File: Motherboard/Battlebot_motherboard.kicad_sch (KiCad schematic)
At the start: 5 parts, among them J1 BEC, U1 rp2040-zero, U2 L9958SBTR, U3 L9958SBTR

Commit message: all the pcb stuff
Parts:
- removed U1: rp2040-zero, footprints:rp2040-zero-tht, symbol mcu:rp2040-zero
- removed U2, U3: L9958SBTR, L9958SBTR:SOP80P1410X360-17N, symbol L9958SBTR:L9958SBTR
- added C10, C9: 1uF, Capacitor_SMD:C_0805_2012Metric_Pad1.18x1.45mm_HandSolder, symbol Device:C
- added C11, C12: 100uF, Capacitor_SMD:CP_Elec_3x5.3, symbol Device:C_Polarized
- added C2, C7, C8: 100nF, Capacitor_SMD:C_0805_2012Metric_Pad1.18x1.45mm_HandSolder, symbol Device:C
- added C3, C4, C5, C6: 10nF, Capacitor_SMD:C_0805_2012Metric_Pad1.18x1.45mm_HandSolder, symbol Device:C
- added J2: Reciever, Connector_PinHeader_2.54mm:PinHeader_1x03_P2.54mm_Vertical, symbol Connector:Conn_01x03_Socket
- added J3: 12Vin, library:2_Wire, symbol Connector:Conn_01x02_Socket
- added J4, J5: Conn_01x02_Socket, library:2_Wire, symbol Connector:Conn_01x02_Socket
- added J6: Fan connector, Connector_JST:JST_PH_S2B-PH-K_1x02_P2.00mm_Horizontal, symbol Connector:Conn_01x02_Socket
- added JP1, JP2: 0ohm, Resistor_SMD:R_1206_3216Metric_Pad1.30x1.75mm_HandSolder, symbol Device:R
- added R1, R2, R5, R6: 10kohm, Resistor_SMD:R_0805_2012Metric_Pad1.20x1.40mm_HandSolder, symbol Device:R
- added R3, R4: 22kohm, Resistor_SMD:R_0805_2012Metric_Pad1.20x1.40mm_HandSolder, symbol Device:R
- added U2, U3: L9958SBTR, POWERSO16_STM, symbol 2024-12-25_01-36-40:L9958SBTR
- added U4: XIAO-RP2040-SMD, footprints:XIAO-RP2040-SMD, symbol Seeed_Studio_XIAO_Series:XIAO-RP2040-SMD
- C1: value C -> 100nF; footprint (none) -> Capacitor_SMD:C_0805_2012Metric_Pad1.18x1.45mm_HandSolder
- J1: footprint (none) -> Connector_PinHeader_2.54mm:PinHeader_1x03_P2.54mm_Vertical
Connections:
- net GND: now also C1.2, C10.2, C11.2, C12.2, C2.2, C7.2, C8.2, C9.2, J2.3 (Pin_3), J3.2 (Pin_2), J6.2 (Pin_2), R3.2, R4.2, R5.2, R6.2, U2.1 (GND), U2.8 (PGND), U3.1 (GND), U3.8 (PGND), U4.16 (GND), U4.20 (GND); no longer J1.2 (Pin_2)
- net +5V: now reaches J1.1 (Pin_1)
- net +5V: now also C7.1, C8.1, J2.1 (Pin_1), J6.1 (Pin_1), R1.2, R2.2, U2.16 (VDD), U3.16 (VDD), U4.14 (5V)
- net PWM3: now reaches J1.3 (Pin_3)
- net PWM3: now also U4.1 (GPIO26_A0_D0)
- net at C1.1: now also U2.4 (CP)
- new net: C5.1, J4.1 (Pin_1)
- new net: C3.2, J4.2 (Pin_2)
- new net: C5.2, U2.10 (OUT2)
- new net: J1.2 (Pin_2), U4.13 (GND)
- new net: C6.2, U3.10 (OUT2)
- new net: R6.1, U3.12 (REXT)
- new net: C2.1, U3.4 (CP)
- new net: C4.1, U3.6 (OUT1)
- new net: R4.1, U3.9 (EN)
- new net: R3.1, U2.9 (EN)
- new net: R5.1, U2.12 (REXT)
- new net: C3.1, U2.6 (OUT1)
- new net: C4.2, J5.2 (Pin_2)
- new net: C6.1, J5.1 (Pin_1)
- new net +12V: C10.1, C11.1, C12.1, C9.1, J3.1 (Pin_1), U2.13 (VS), U3.13 (VS)
- new net 1SO: U2.14 (SI), U3.2 (SO)
- new net CS: U2.3 (CS), U3.3 (CS), U4.8 (GPIO1_D7_CSn_RX)
- new net DI1: R2.1, U3.7 (DI)
- new net DI2: R1.1, U2.7 (DI)
- new net DIR1: U3.5 (DIR), U4.5 (GPIO6_D4_SDA)
- new net DIR2: U2.5 (DIR), U4.6 (GPIO7_D5_SCL)
- new net PPM: J2.2 (Pin_2), U4.4 (GPIO29_A3_D3)
- new net PWM1: U3.11 (PWM), U4.2 (GPIO27_A1_D1)
- new net PWM2: U2.11 (PWM), U4.3 (GPIO28_A2_D2)
- new net SCK: U2.15 (SCK), U3.15 (SCK), U4.9 (GPIO2_D8_SCK)
- new net µSI: U2.2 (SO), U4.11 (GPIO3_D10_MOSI)
- new net µSO: U3.14 (SI), U4.10 (GPIO4_D9_MISO)
- no-connect marks 0 -> 7
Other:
- note added: "Brushed Motor Drivers"
- note added: "Microcontroller"
- note added: "Misc. Connectors"

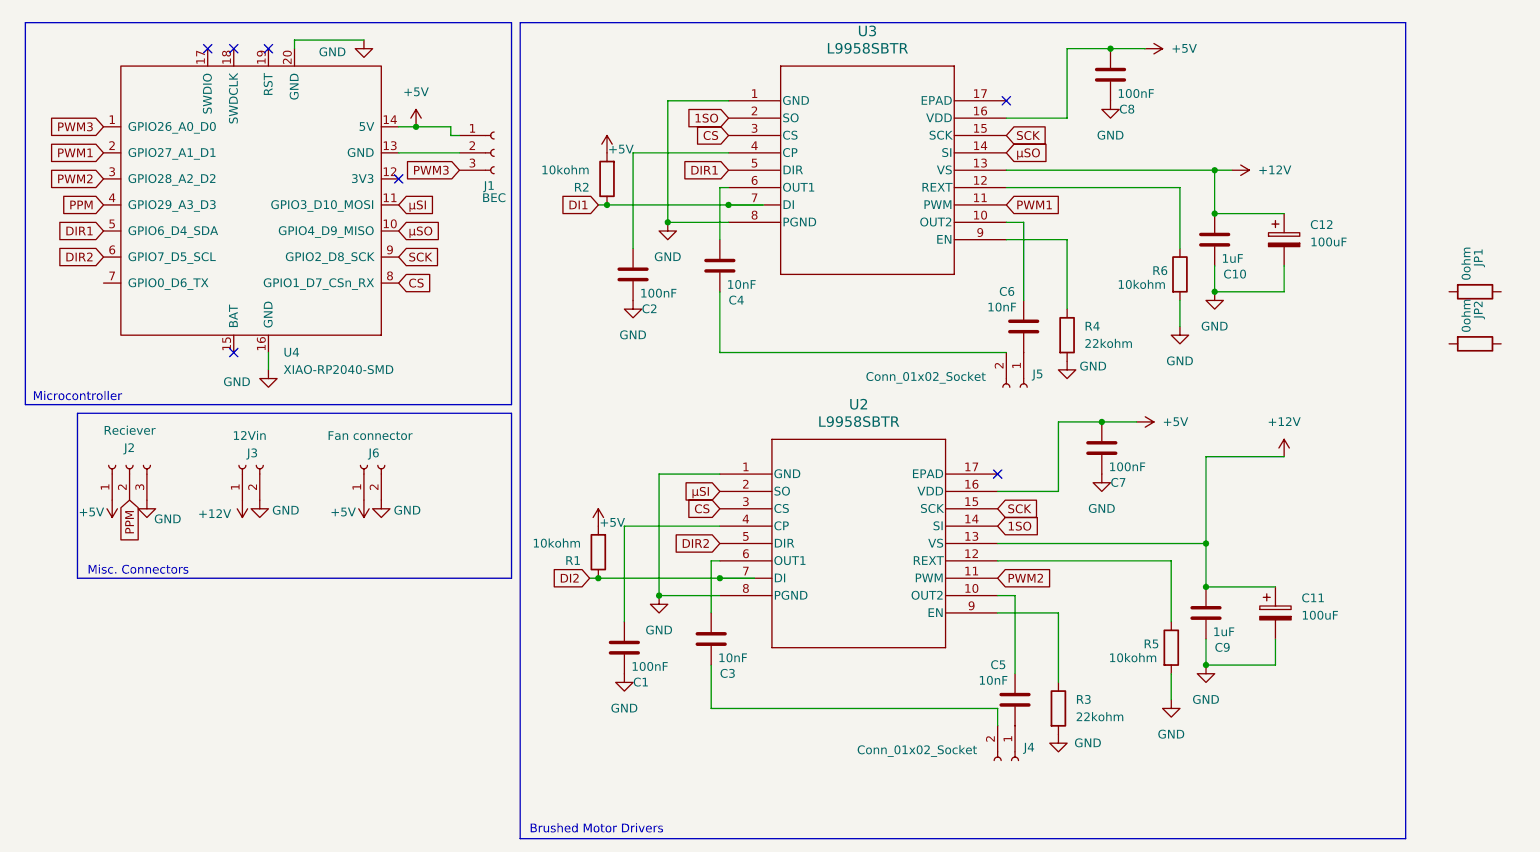
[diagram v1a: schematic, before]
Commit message: Update schematic which was quite wrong in a number of places
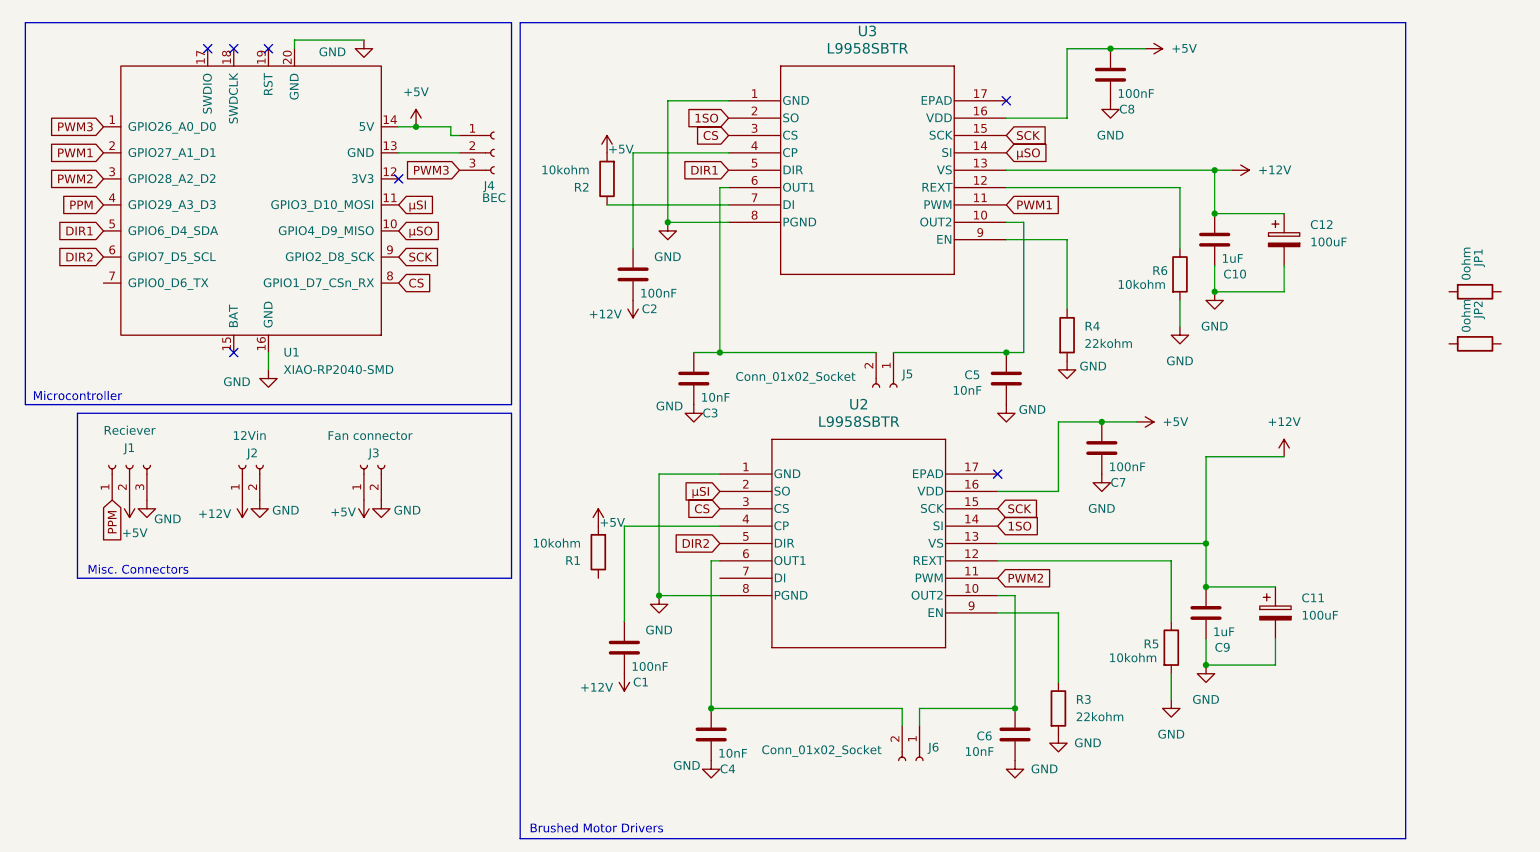
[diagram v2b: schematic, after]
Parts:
- renumbered C4 to C3, C3 to C4, C6 to C5, C5 to C6, J2 to J1, J3 to J2, J6 to J3, J1 to J4, J4 to J6, U4 to U1
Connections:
- net +12V: now also C1.2, C2.2
- net +5V: now also J1.2 (Pin_2); no longer J1.1 (Pin_1)
- net GND: now also C3.2, C4.2, C5.1, C6.1; no longer C1.2, C2.2
- net PPM: now also J1.1 (Pin_1); no longer J1.2 (Pin_2)
- net at J6.1 (Pin_1): now also C6.2, U2.10 (OUT2); no longer C6.1
- net at J6.2 (Pin_2): now also C4.1, U2.6 (OUT1); no longer C4.2
- net at C5.2, U3.10 (OUT2): now also J5.1 (Pin_1)
- net at C3.1, U3.6 (OUT1): now also J5.2 (Pin_2)
- net DI1: no longer names the net of R2.1, U3.7 (DI)
- net DI2: no longer names the net of U2.7 (DI)
- net DI2: no longer R1.1
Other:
- moved on the sheet: C3, C4, C5, C6, J5, J6

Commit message: nightmare routing job
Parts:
- J5, J6: footprint library:2_Wire -> Connector_JST:JST_PH_S2B-PH-K_1x02_P2.00mm_Horizontal
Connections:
- net GND: now also U2.17 (EPAD), U3.17 (EPAD)
- net at U2.7 (DI): now also R1.1
- no-connect marks 7 -> 5
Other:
- moved on the sheet: R1
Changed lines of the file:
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@@
 	)
 	(no_connect
-		(at 154.94 81.28)
-	)
-	(no_connect
-		(at 156.21 26.67)
-	)
-	(no_connect
 		(at 48.26 19.05)
 	)
@@
 	(wire
 		(pts
+			(xy 96.52 96.52) (xy 114.3 96.52)
+		)
+		(stroke
+			(width 0)
+			(type default)
+		)
+	)
+	(wire
+		(pts
 			(xy 110.49 63.5) (xy 114.3 63.5)
 		)
@@
 			)
 		)
-		(property "Footprint" "library:2_Wire"
+		(property "Footprint" "Connector_JST:JST_PH_S2B-PH-K_1x02_P2.00mm_Horizontal"
 			(at 143.51 123.19 0)
 			(effects
@@
 	(symbol
 		(lib_id "Device:R")
-		(at 96.52 92.71 180)
+		(at 96.52 92.71 0)
+		(mirror x)
 		(unit 1)
 		(exclude_from_sim no)
@@
 		(dnp no)
 		(property "Reference" "R1"
-			(at 93.98 93.9801 0)
+			(at 99.06 93.9801 0)
 			(effects
 				(font
@@
 		)
 		(property "Value" "10kohm"
-			(at 93.98 91.4401 0)
+			(at 99.06 91.4401 0)
 			(effects
 				(font
@@
 		)
 		(property "Footprint" "Resistor_SMD:R_0805_2012Metric_Pad1.20x1.40mm_HandSolder"
-			(at 98.298 92.71 90)
+			(at 94.742 92.71 90)
 			(effects
 				(font
@@
 	)
 	(symbol
+		(lib_id "power:GND")
+		(at 156.21 26.67 180)
+		(unit 1)
+		(exclude_from_sim no)
+		(in_bom yes)
+		(on_board yes)
+		(dnp no)
+		(fields_autoplaced yes)
+		(property "Reference" "#PWR032"
+			(at 156.21 20.32 0)
+			(effects
+				(font
+					(size 1.27 1.27)
+				)
+				(hide yes)
+			)
+		)
+		(property "Value" "GND"
+			(at 156.21 21.59 0)
+			(effects
+				(font
+					(size 1.27 1.27)
+				)
+			)
+		)
+		(property "Footprint" ""
+			(at 156.21 26.67 0)
+			(effects
+				(font
+					(size 1.27 1.27)
+				)
+				(hide yes)
+			)
+		)
+		(property "Datasheet" ""
+			(at 156.21 26.67 0)
+			(effects
+				(font
+					(size 1.27 1.27)
+				)
+				(hide yes)
+			)
+		)
+		(property "Description" "Power symbol creates a global label with name \"GND\" , ground"
+			(at 156.21 26.67 0)
+			(effects
+				(font
+					(size 1.27 1.27)
+				)
+				(hide yes)
+			)
+		)
+		(pin "1"
+		)
+		(instances
+			(project ""
+				(path "/1991c32d-5f82-4678-bacc-ea14347159fa"
+					(reference "#PWR032")
+					(unit 1)
+				)
+			)
+		)
+	)
+	(symbol
 		(lib_id "Device:C")
 		(at 185.42 101.6 0)
@@
 			)
 		)
-		(property "Footprint" "library:2_Wire"
+		(property "Footprint" "Connector_JST:JST_PH_S2B-PH-K_1x02_P2.00mm_Horizontal"
 			(at 139.7 68.58 0)
 			(effects
@@
 					(unit 1)
 				)
+			)
+		)
+	)
+	(symbol
+		(lib_id "power:GND")
+		(at 154.94 81.28 180)
+		(unit 1)
+		(exclude_from_sim no)
+		(in_bom yes)
+		(on_board yes)
+		(dnp no)
+		(fields_autoplaced yes)
+		(property "Reference" "#PWR033"
+			(at 154.94 74.93 0)
+			(effects
+				(font
+					(size 1.27 1.27)
+				)
+				(hide yes)
+			)
+		)
+		(property "Value" "GND"
+			(at 154.94 76.2 0)
+			(effects
+				(font
+					(size 1.27 1.27)
+				)
+			)
+		)
+		(property "Footprint" ""
+			(at 154.94 81.28 0)
+			(effects
+				(font
+					(size 1.27 1.27)
+				)
+				(hide yes)
+			)
+		)
+		(property "Datasheet" ""
+			(at 154.94 81.28 0)
+			(effects
+				(font
+					(size 1.27 1.27)
+				)
+				(hide yes)
+			)
+		)
+		(property "Description" "Power symbol creates a global label with name \"GND\" , ground"
+			(at 154.94 81.28 0)
+			(effects
+				(font
+					(size 1.27 1.27)
+				)
+				(hide yes)
+			)
+		)
+		(pin "1"
+		)
+		(instances
+			(project "Battlebot_motherboard"
+				(path "/1991c32d-5f82-4678-bacc-ea14347159fa"
+					(reference "#PWR033")
+					(unit 1)
+				)

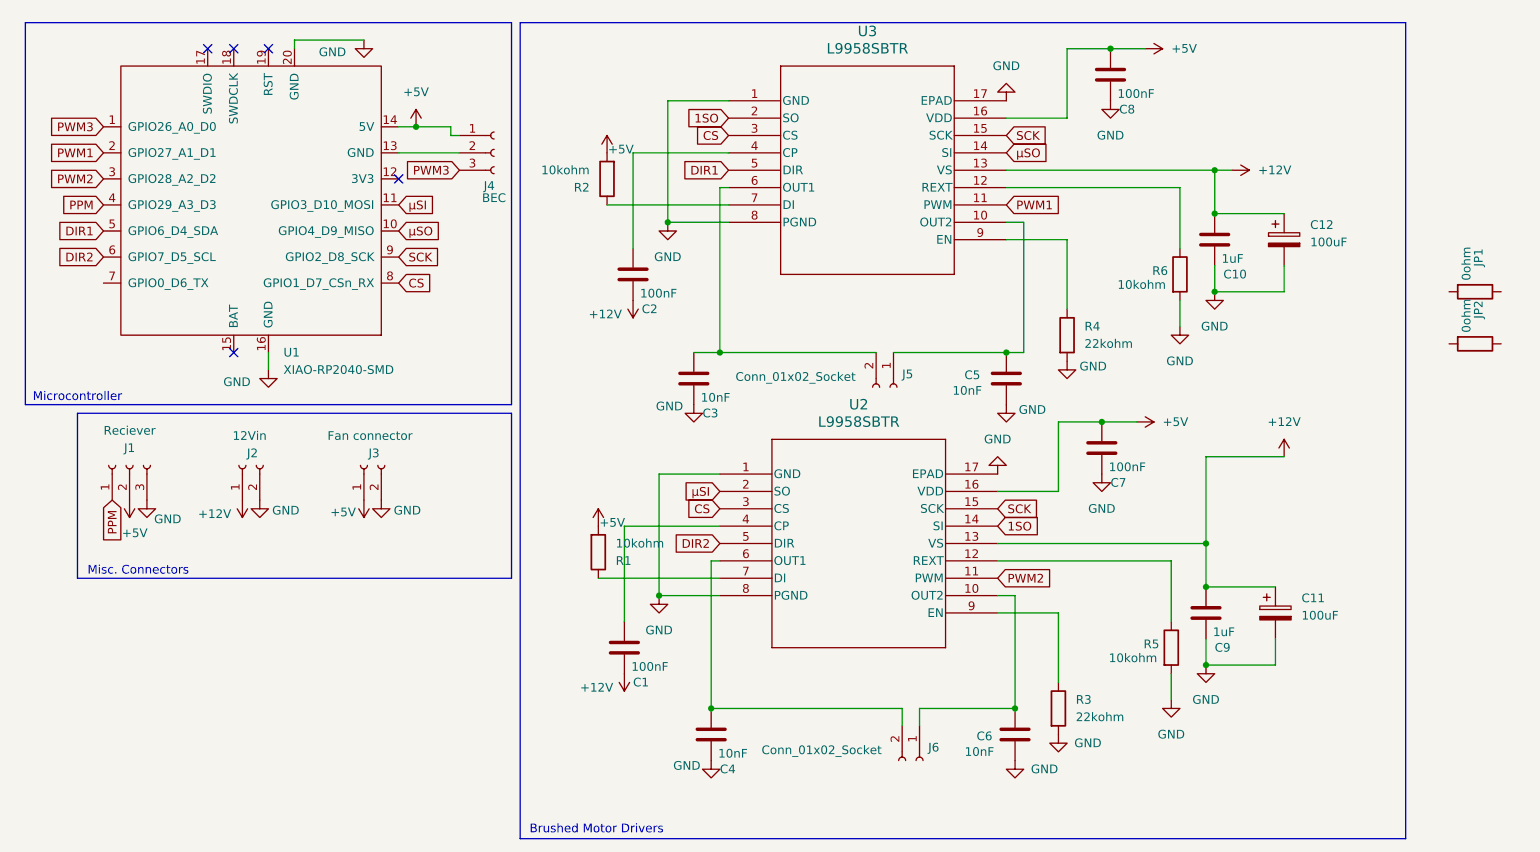
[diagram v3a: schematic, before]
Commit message: reroute using 2 layers and fix 1 connector
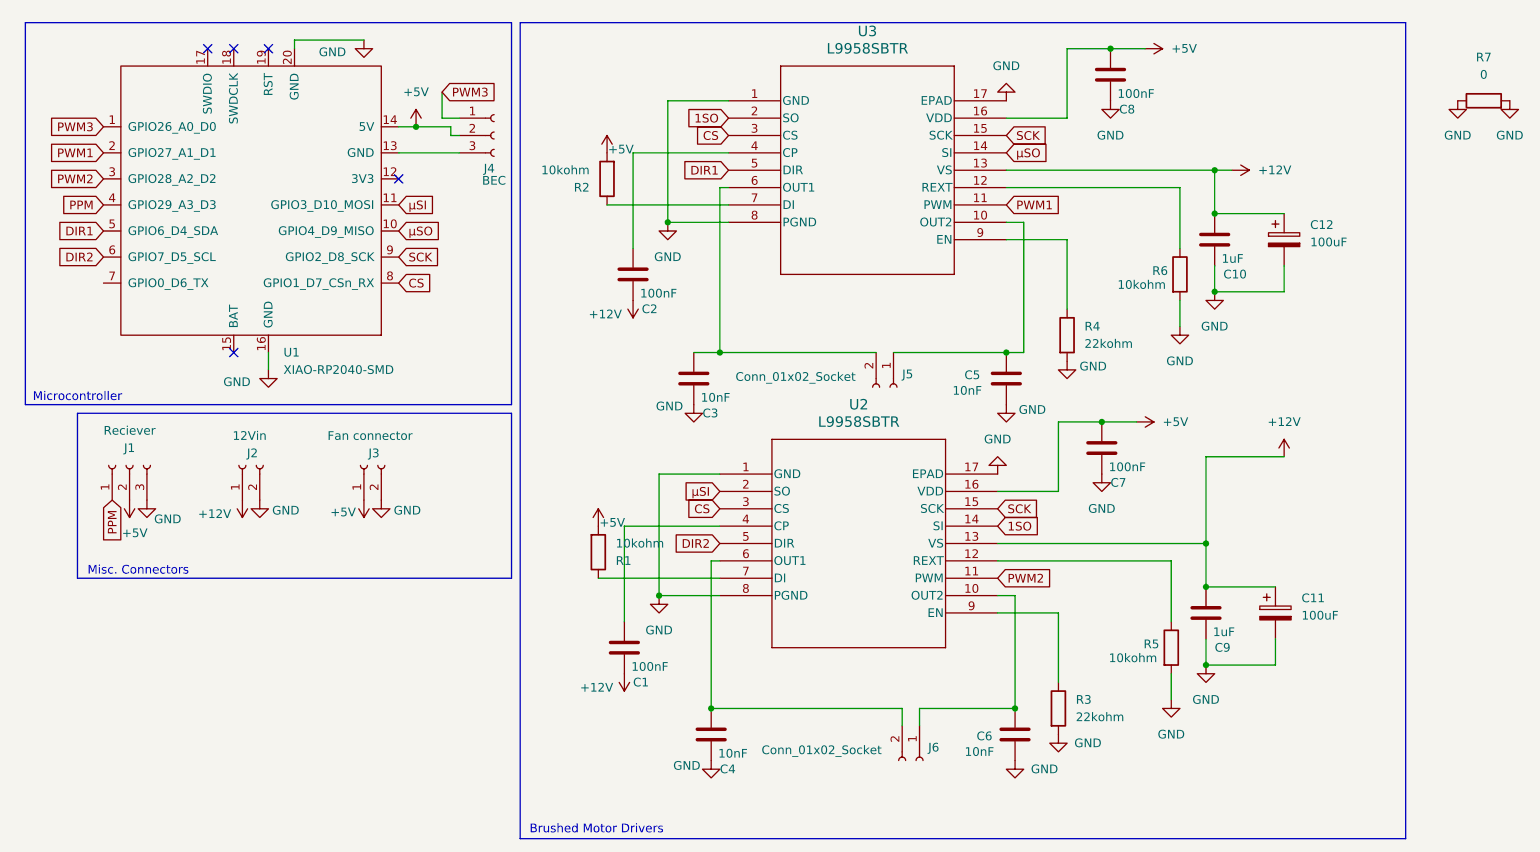
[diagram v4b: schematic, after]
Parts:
- removed JP1, JP2: 0ohm, Resistor_SMD:R_1206_3216Metric_Pad1.30x1.75mm_HandSolder, symbol Device:R
- added R7: 0, Resistor_THT:R_Axial_DIN0204_L3.6mm_D1.6mm_P5.08mm_Vertical, symbol Device:R
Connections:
- net +5V: now also J4.2 (Pin_2); no longer J4.1 (Pin_1)
- net GND: now also R7.1, R7.2
- net PWM3: now also J4.1 (Pin_1); no longer J4.3 (Pin_3)
- net at U1.13 (GND): now also J4.3 (Pin_3); no longer J4.2 (Pin_2)
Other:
- moved on the sheet: J4

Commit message: new cap footprint and rerouting for it
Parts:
- C11, C12: footprint Capacitor_SMD:CP_Elec_3x5.3 -> footprints:CAP_UCD_4X5P8_NCH
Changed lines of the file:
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@@
 			)
 		)
-		(property "Footprint" "Capacitor_SMD:CP_Elec_3x5.3"
+		(property "Footprint" "footprints:CAP_UCD_4X5P8_NCH"
 			(at 196.5452 105.41 0)
 			(effects
@@
 			)
 		)
-		(property "Footprint" "Capacitor_SMD:CP_Elec_3x5.3"
+		(property "Footprint" "footprints:CAP_UCD_4X5P8_NCH"
 			(at 197.8152 50.8 0)
 			(effects

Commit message: fix traces and stuff
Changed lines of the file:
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@@
 (kicad_sch
-	(version 20231120)
+	(version 20250114)
 	(generator "eeschema")
-	(generator_version "8.0")
+	(generator_version "9.0")
 	(paper "A4")
+	(rectangle
+		(start 20.32 72.39)
+		(end 83.82 96.52)
+		(stroke
+			(width 0)
+			(type default)
+		)
+		(fill
+			(type none)
+		)
+	)
+	(rectangle
+		(start 85.09 15.24)
+		(end 214.63 134.62)
+		(stroke
+			(width 0)
+			(type default)
+		)
+		(fill
+			(type none)
+		)
+	)
+	(rectangle
+		(start 12.7 15.24)
+		(end 83.82 71.12)
+		(stroke
+			(width 0)
+			(type default)
+		)
+		(fill
+			(type none)
+		)
+	)
+	(text "Misc. Connectors"
+		(exclude_from_sim no)
+		(at 29.21 95.504 0)
+		(effects
+			(font
+				(size 1.27 1.27)
+			)
+		)
+	)
+	(text "Microcontroller"
+		(exclude_from_sim no)
+		(at 20.32 70.104 0)
+		(effects
+			(font
+				(size 1.27 1.27)
+			)
+		)
+	)
+	(text "Brushed Motor Drivers\n"
+		(exclude_from_sim no)
+		(at 96.266 133.35 0)
+		(effects
+			(font
+				(size 1.27 1.27)
+			)
+		)
+	)
 	(junction
 		(at 171.45 19.05)
@@
 		)
 	)
-	(rectangle
-		(start 20.32 72.39)
-		(end 83.82 96.52)
-		(stroke
-			(width 0)
-			(type default)
-		)
-		(fill
-			(type none)
-		)
-	)
-	(rectangle
-		(start 85.09 15.24)
-		(end 214.63 134.62)
-		(stroke
-			(width 0)
-			(type default)
-		)
-		(fill
-			(type none)
-		)
-	)
-	(rectangle
-		(start 12.7 15.24)
-		(end 83.82 71.12)
-		(stroke
-			(width 0)
-			(type default)
-		)
-		(fill
-			(type none)
-		)
-	)
-	(text "Misc. Connectors"
-		(exclude_from_sim no)
-		(at 29.21 95.504 0)
-		(effects
-			(font
-				(size 1.27 1.27)
-			)
-		)
-	)
-	(text "Microcontroller"
-		(exclude_from_sim no)
-		(at 20.32 70.104 0)
-		(effects
-			(font
-				(size 1.27 1.27)
-			)
-		)
-	)
-	(text "Brushed Motor Drivers\n"
-		(exclude_from_sim no)
-		(at 96.266 133.35 0)
-		(effects
-			(font
-				(size 1.27 1.27)
-			)
-		)
-	)
 	(global_label "PWM1"
 		(shape input)
@@
 		)
 	)
+	(embedded_fonts no)
 )
